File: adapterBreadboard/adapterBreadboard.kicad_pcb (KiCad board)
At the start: 2 copper layers, 60 x 60 mm, 12 parts, among them J101 USB, K101 PWR, K102 CONN_3, P101 CONN_19, P102 CONN_19, P103 CONN_2, SW101 Boot0, SW102 Reset

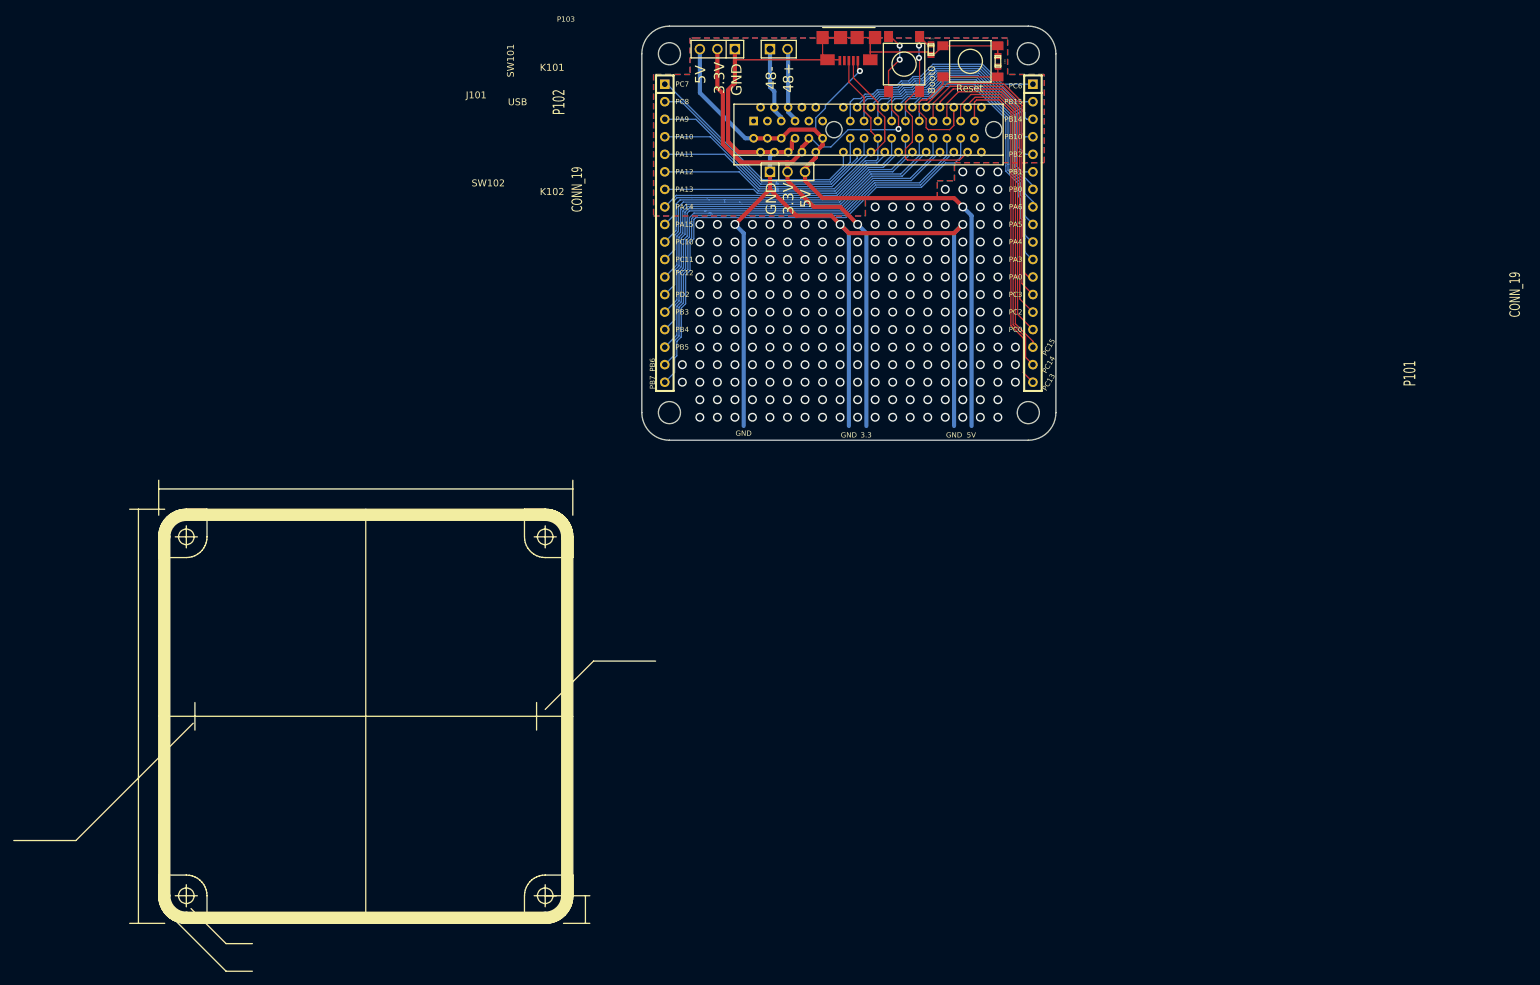
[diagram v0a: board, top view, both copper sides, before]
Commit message: As ordered the first time, but with a fix for the resistor
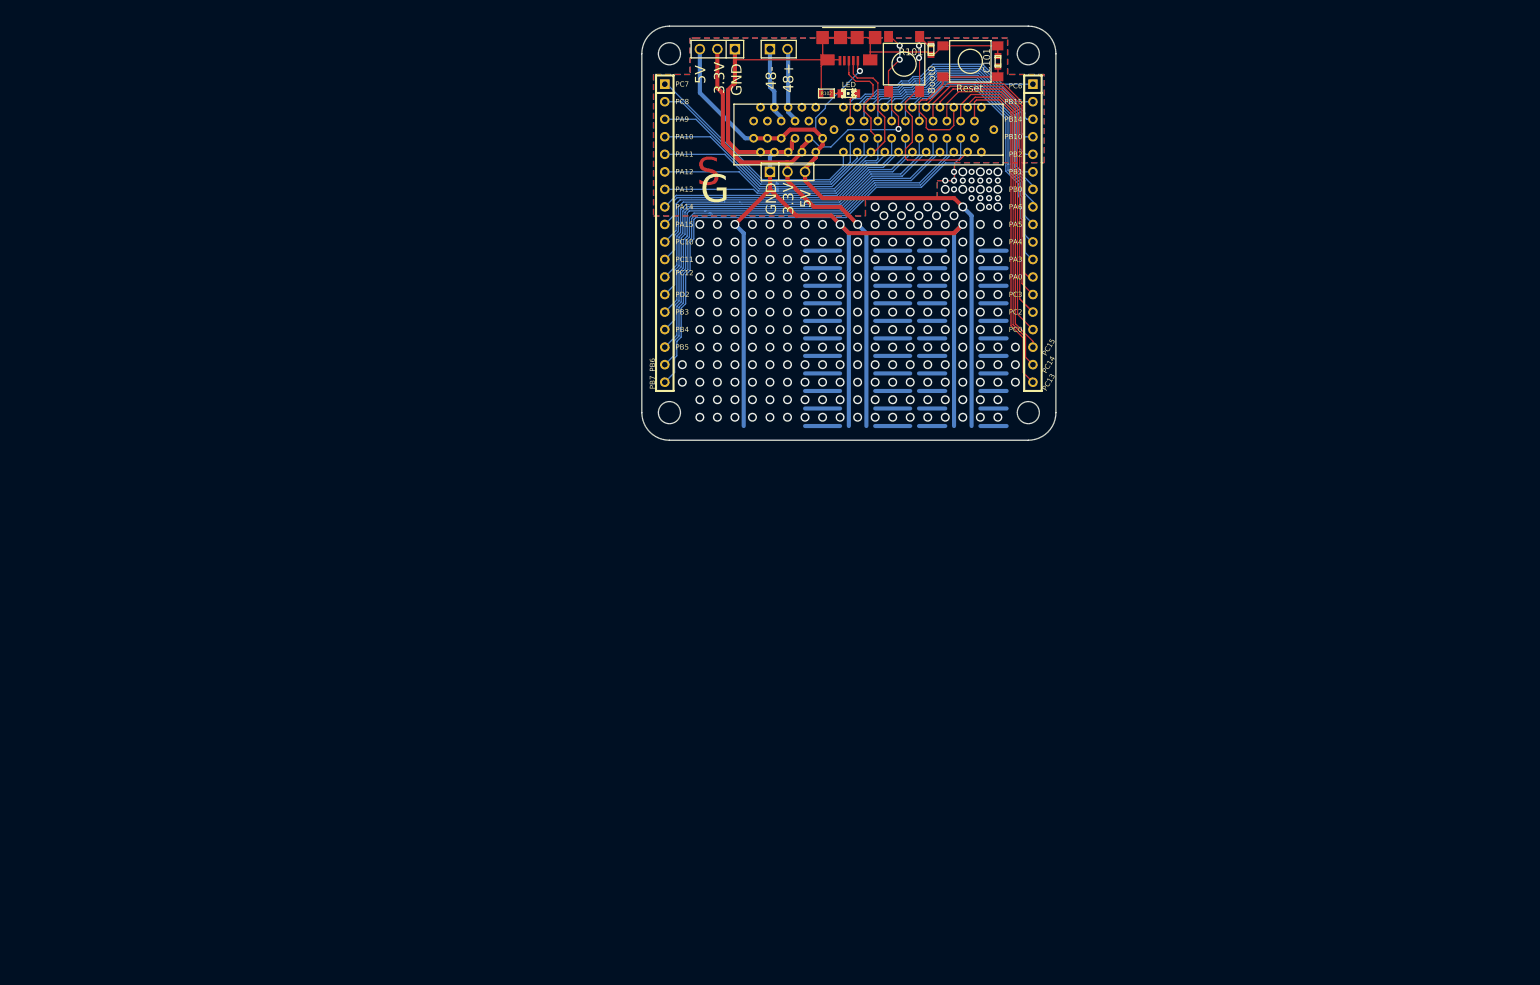
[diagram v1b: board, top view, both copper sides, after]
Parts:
- removed 60mm: 60mm, dp_devices-DP6060_V1
- added D101: LED, LED-0805, F.Cu at (235.0, 117.8)
- added R102: 220, SM0603, F.Cu at (231.8, 117.8)
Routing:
- net (no net): track 0.00 -> 195.6 mm, vias 231 -> 254
- net GND: track 209.3 -> 214.5 mm
- net /PC6: track 32.7 -> 37.0 mm
- net /PA12: track 50.6 -> 52.9 mm
- net N-0000042: track 0.00 -> 1.44 mm
- net /PA11: track 50.9 -> 52.3 mm
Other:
- board text added: "G"
- board text added: "S"
